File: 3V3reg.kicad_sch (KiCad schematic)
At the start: 2 parts, among them U2 LM2594M-3.3

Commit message: first commit!!!
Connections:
- net PP_3V3_MAIN: now also U2.7 (VIN)
- net PP_USBC_VBUS: now also U2.5 (~{ON}/OFF)
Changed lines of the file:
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@@
+		)
+	)
+	(wire
+		(pts
+			(xy 95.25 96.52) (xy 124.46 96.52)
+		)
+		(stroke
+			(width 0)
+			(type default)
+		)
+	)
+	(wire
+		(pts
+			(xy 95.25 101.6) (xy 95.25 96.52)
+		)
+		(stroke
+			(width 0)
+			(type default)
+		)
+	)
+	(wire
+		(pts
+			(xy 100.33 93.98) (xy 124.46 93.98)
+		)
+		(stroke
+			(width 0)
+			(type default)
+		)
+	)
+	(wire
+		(pts
+			(xy 91.44 101.6) (xy 95.25 101.6)
+		)
+		(stroke
+			(width 0)
+			(type default)
 		)
 	)
@@
 	(hierarchical_label "PP_USBC_VBUS"
 		(shape input)
-		(at 195.58 95.25 0)
+		(at 91.44 101.6 180)
 		(effects
 			(font
 				(size 1.27 1.27)
 			)
-			(justify left)
+			(justify right)
 		)
 	)

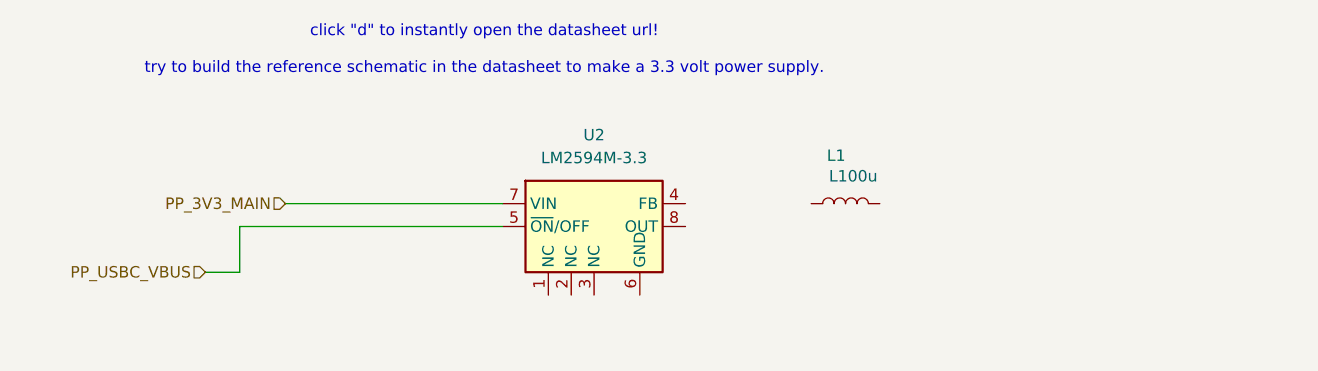
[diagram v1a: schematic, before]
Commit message: Create power regulator schematic
Signed-off-by: sanyue <sanyue7th@gmail.com>
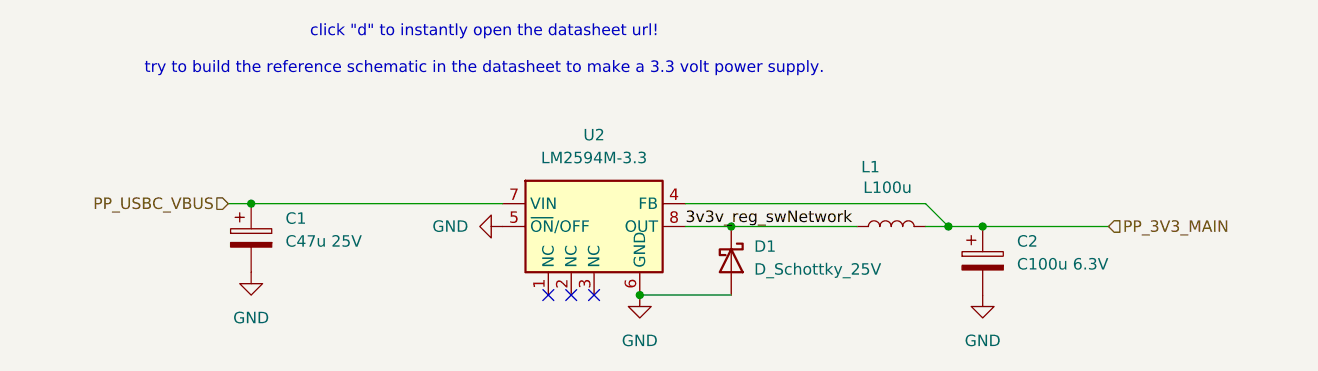
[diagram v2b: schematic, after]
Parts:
- added C1: C47u 25V, symbol Device:C_Polarized
- added C2: C100u 6.3V, symbol Device:C_Polarized
- added D1: D_Schottky_25V, symbol Device:D_Schottky
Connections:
- net PP_3V3_MAIN: now also L1.2, U2.4 (FB), C2.1; no longer U2.7 (VIN)
- net PP_USBC_VBUS: now also U2.7 (VIN), C1.1; no longer U2.5 (~{ON}/OFF)
- net 3v3v_reg_swNetwork: now reaches L1.1
- net 3v3v_reg_swNetwork: now also U2.8 (OUT), D1.1 (K)
- net GND: now reaches U2.6 (GND)
- net GND: now also U2.5 (~{ON}/OFF), C1.2, C2.2, D1.2 (A)
- no-connect marks 0 -> 3
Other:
- moved on the sheet: L1

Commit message: added lcsc, datasheet, and footprint. couldn't find zener and polarized stuff tho
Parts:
- C1, C2: footprint (none) -> Capacitor_SMD:C_0201_0603Metric; LCSC (none) -> C14663
- D1: footprint (none) -> Diode_SMD:D_2114_3652Metric; LCSC (none) -> C466507
- L1: footprint (none) -> Inductor_SMD:L_0201_0603Metric; LCSC (none) -> C162581
- U2: LCSC (none) -> C316691
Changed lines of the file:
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@@
 			)
 		)
-		(property "Footprint" ""
+		(property "Footprint" "Inductor_SMD:L_0201_0603Metric"
 			(at 167.64 96.52 0)
 			(effects
@@
 			)
 		)
-		(property "Datasheet" "~"
+		(property "Datasheet" "https://www.lcsc.com/datasheet/lcsc_datasheet_2410121957_Murata-Electronics-LQM18PN3R3MFRL_C162581.pdf"
 			(at 167.64 96.52 0)
 			(effects
@@
 			)
 		)
+		(property "LCSC" "C162581"
+			(at 167.64 96.52 90)
+			(effects
+				(font
+					(size 1.27 1.27)
+				)
+				(hide yes)
+			)
+		)
 		(pin "1"
 		)
@@
 			)
 		)
-		(property "Footprint" ""
+		(property "Footprint" "Capacitor_SMD:C_0201_0603Metric"
 			(at 97.4852 101.6 0)
 			(effects
@@
 			)
 		)
-		(property "Datasheet" "~"
+		(property "Datasheet" "https://www.lcsc.com/datasheet/lcsc_datasheet_2211101700_YAGEO-CC0603KRX7R9BB104_C14663.pdf"
 			(at 96.52 97.79 0)
 			(effects
@@
 			)
 		)
+		(property "LCSC" "C14663"
+			(at 96.52 97.79 0)
+			(effects
+				(font
+					(size 1.27 1.27)
+				)
+				(hide yes)
+			)
+		)
 		(pin "1"
 		)
@@
 			)
 		)
-		(property "Footprint" ""
+		(property "Footprint" "Diode_SMD:D_2114_3652Metric"
 			(at 149.86 100.33 0)
 			(effects
@@
 			)
 		)
-		(property "Datasheet" "~"
+		(property "Datasheet" "https://www.lcsc.com/datasheet/lcsc_datasheet_2410121321_High-Diode-SS520_C466507.pdf"
 			(at 149.86 100.33 0)
 			(effects
@@
 			)
 		)
+		(property "LCSC" "C466507"
+			(at 149.86 100.33 90)
+			(effects
+				(font
+					(size 1.27 1.27)
+				)
+				(hide yes)
+			)
+		)
 		(pin "2"
 		)
@@
 			)
 		)
+		(property "LCSC" "C316691"
+			(at 134.62 96.52 0)
+			(effects
+				(font
+					(size 1.27 1.27)
+				)
+				(hide yes)
+			)
+		)
 		(pin "4"
 		)
@@
 			)
 		)
-		(property "Footprint" ""
+		(property "Footprint" "Capacitor_SMD:C_0201_0603Metric"
 			(at 178.7652 104.14 0)
 			(effects
@@
 			)
 		)
-		(property "Datasheet" "~"
+		(property "Datasheet" "https://www.lcsc.com/datasheet/lcsc_datasheet_2211101700_YAGEO-CC0603KRX7R9BB104_C14663.pdf"
 			(at 177.8 100.33 0)
 			(effects
@@
 			(at 177.8 100.33 0)
 			(effects
+				(font
+					(size 1.27 1.27)
+				)
+				(hide yes)
+			)
+		)
+		(property "LCSC" "C14663"
+			(at 177.8 100.33 0)
+			(effects

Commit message: cinna 4 more circuit
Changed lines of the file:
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@@
 		)
 	)
-	(hierarchical_label "PP_USBC_VBUS"
-		(shape input)
-		(at 93.98 93.98 180)
+	(label "PP_USBC_VBUS"
+		(at 93.98 93.98 0)
 		(effects
 			(font
 				(size 1.27 1.27)
 			)
-			(justify right)
+			(justify left bottom)
 		)
 	)

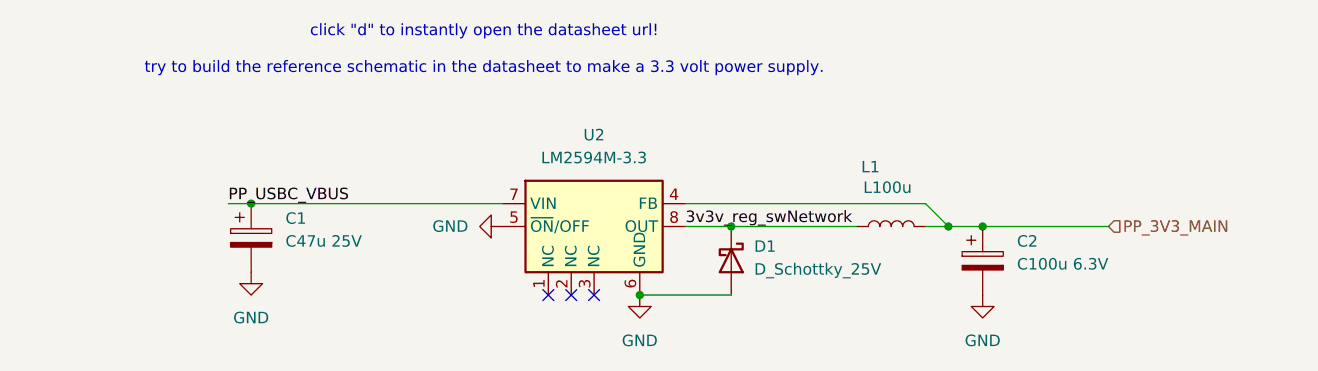
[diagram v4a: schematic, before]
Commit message: Cleanup, add 5vREG block
Signed-off-by: sanyue <sanyue7th@gmail.com>
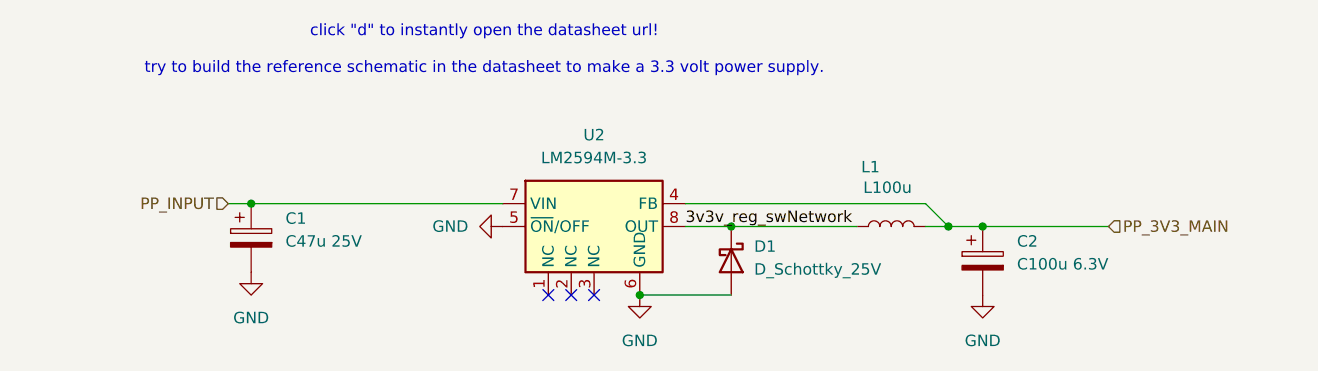
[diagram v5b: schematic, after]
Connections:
- net PP_USBC_VBUS renamed PP_INPUT
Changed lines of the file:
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@@
 		)
 	)
-	(label "PP_USBC_VBUS"
-		(at 93.98 93.98 0)
+	(hierarchical_label "PP_INPUT"
+		(shape input)
+		(at 93.98 93.98 180)
 		(effects
 			(font
 				(size 1.27 1.27)
 			)
-			(justify left bottom)
+			(justify right)
 		)
 	)
